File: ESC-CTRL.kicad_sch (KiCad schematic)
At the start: 42 parts, among them P1 V, P2 G, P3 TX, P4 RX, P5 D, P6 K, U1 AT32F413KCU7-4, U2 GM7333

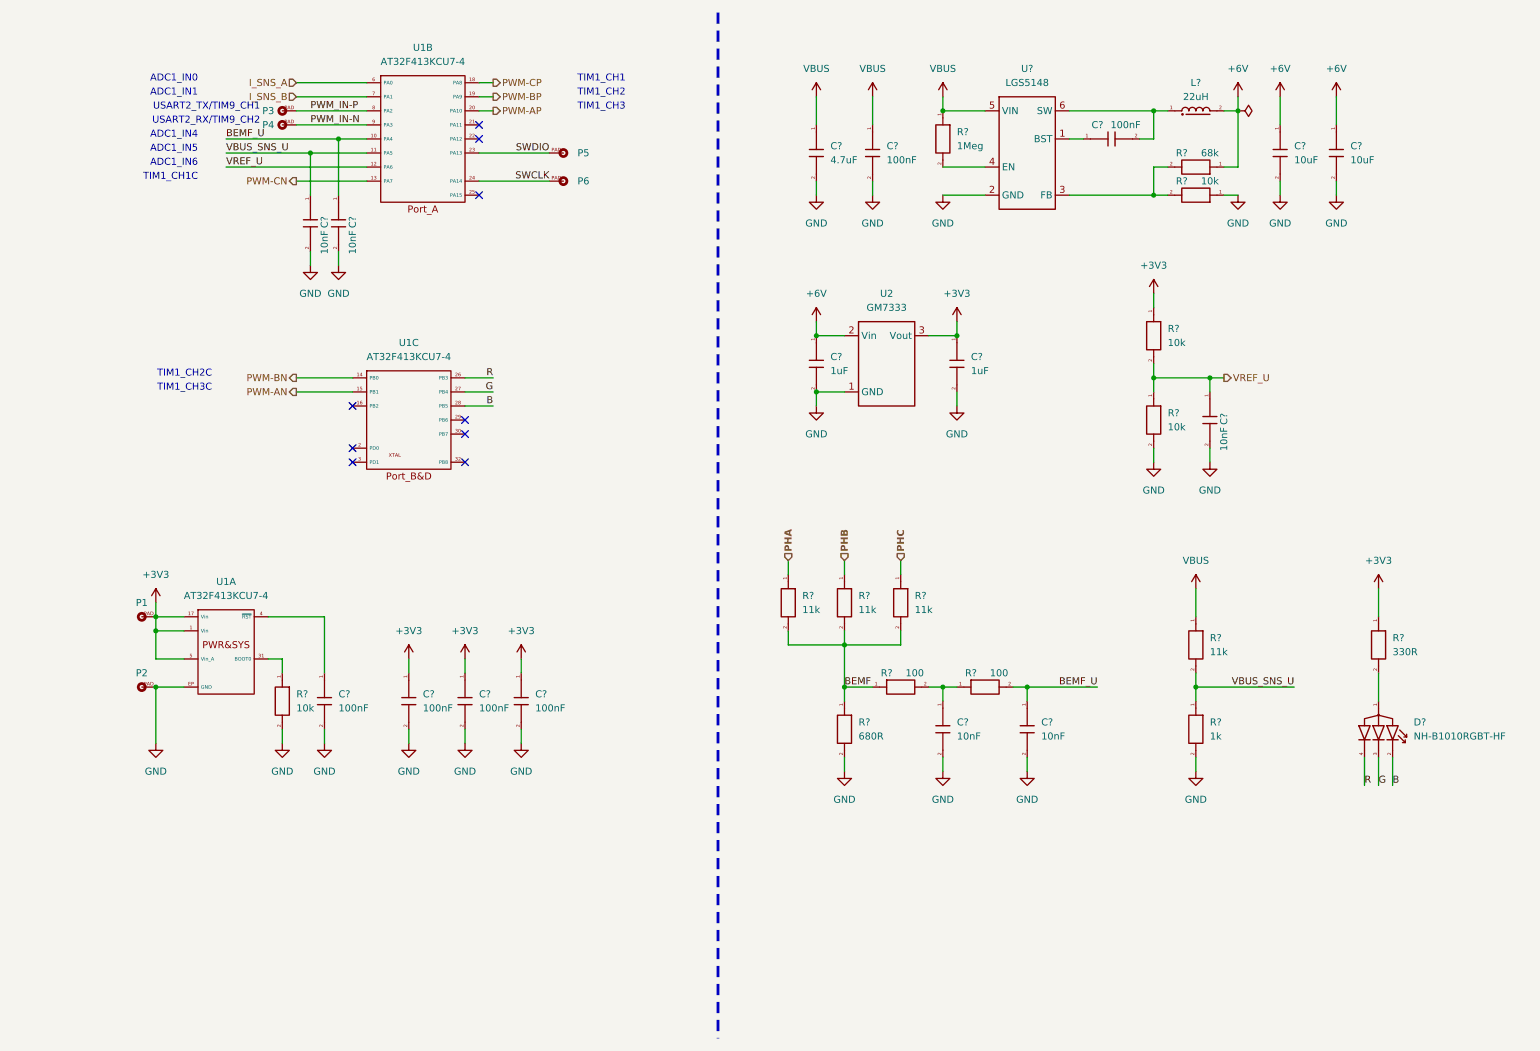
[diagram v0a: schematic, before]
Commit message: Update layout and modified sense amplifier
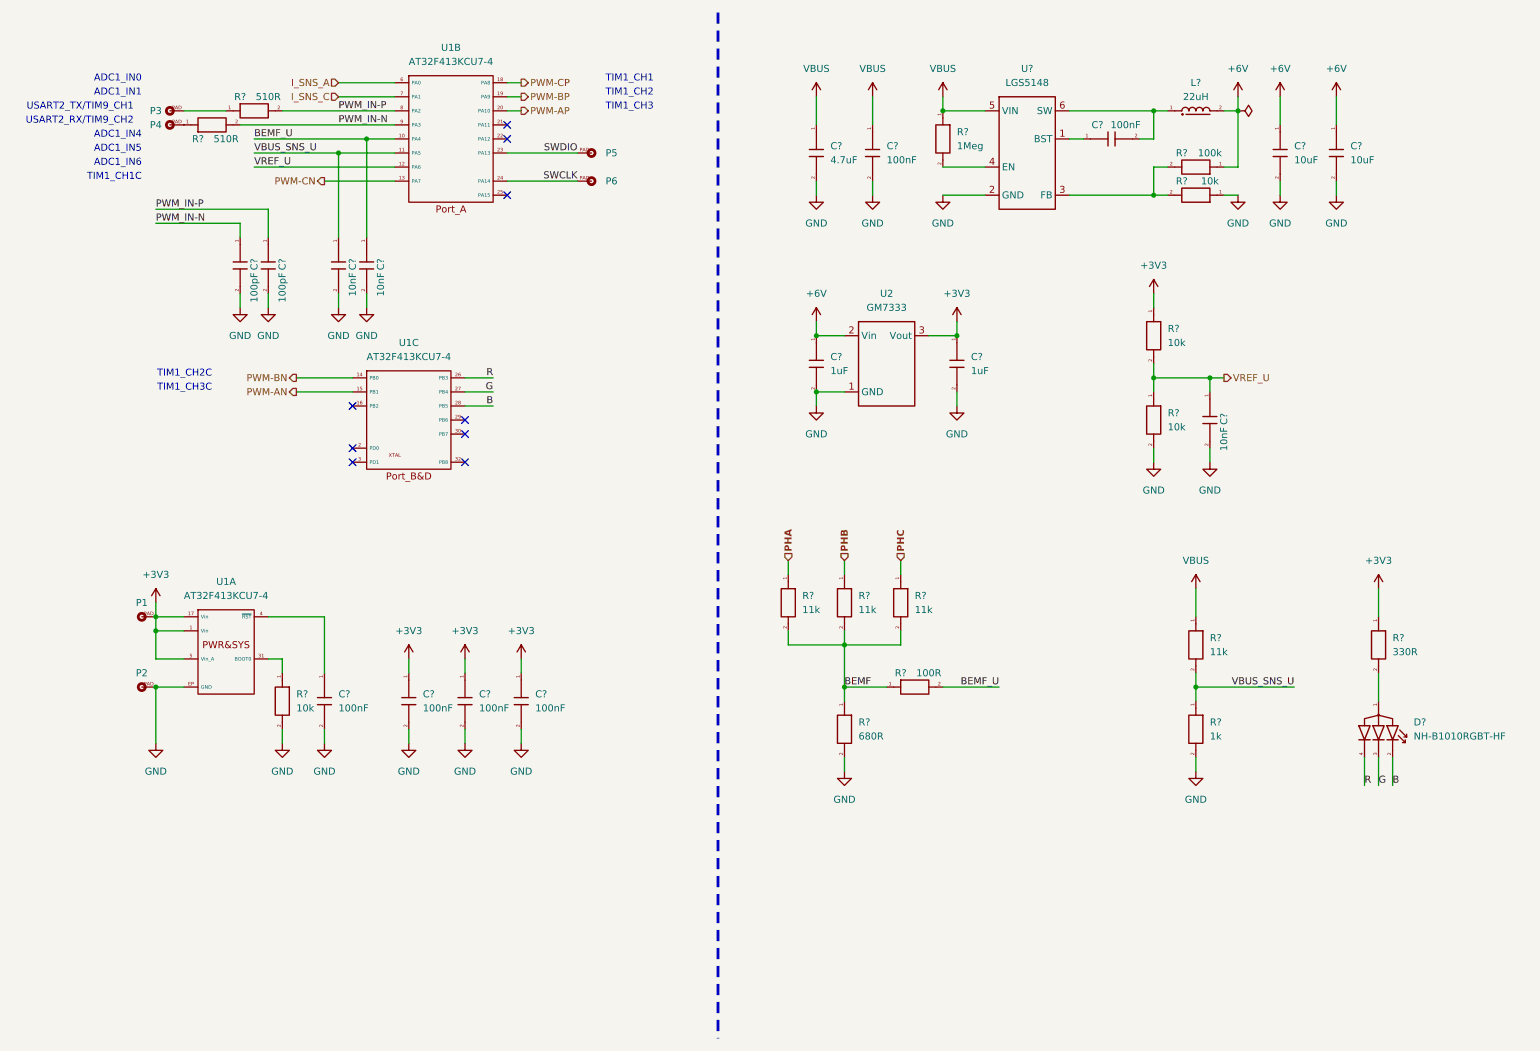
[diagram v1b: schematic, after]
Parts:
- removed C? (x2): 10nF, 001_GN_RCL_SMD:C0201(0603M), symbol 001_Basic_PassiveComponents:101_Capacitor
- removed R? (x2): 100, 001_GN_RCL_SMD:R0201(0603M), symbol 001_Basic_PassiveComponents:001_Resistor
- added C? (x2): 100pF, 001_GN_RCL_SMD:C0201(0603M), symbol 001_Basic_PassiveComponents:101_Capacitor
- added R?: 100R, 001_GN_RCL_SMD:R0201(0603M), symbol 001_Basic_PassiveComponents:001_Resistor
- added R? (x2): 510R, 001_GN_RCL_SMD:R0201(0603M), symbol 001_Basic_PassiveComponents:001_Resistor
- R?: value 68k -> 100k
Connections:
- net BEMF: now also R?.1
- net BEMF_U: now also R?.2
- net GND: now also C?.2, C?.2
- net PWM_IN-N: now also C?.1, R?.2; no longer P4.PAD
- net PWM_IN-P: now also C?.1, R?.2; no longer P3.PAD
- net I_SNS_B renamed I_SNS_C
- new net: P4.PAD, R?.1
- new net: P3.PAD, R?.1
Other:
- moved on the sheet: C?, P3, P4, P5, P6, U1B

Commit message: Modified the scheme of current sensing
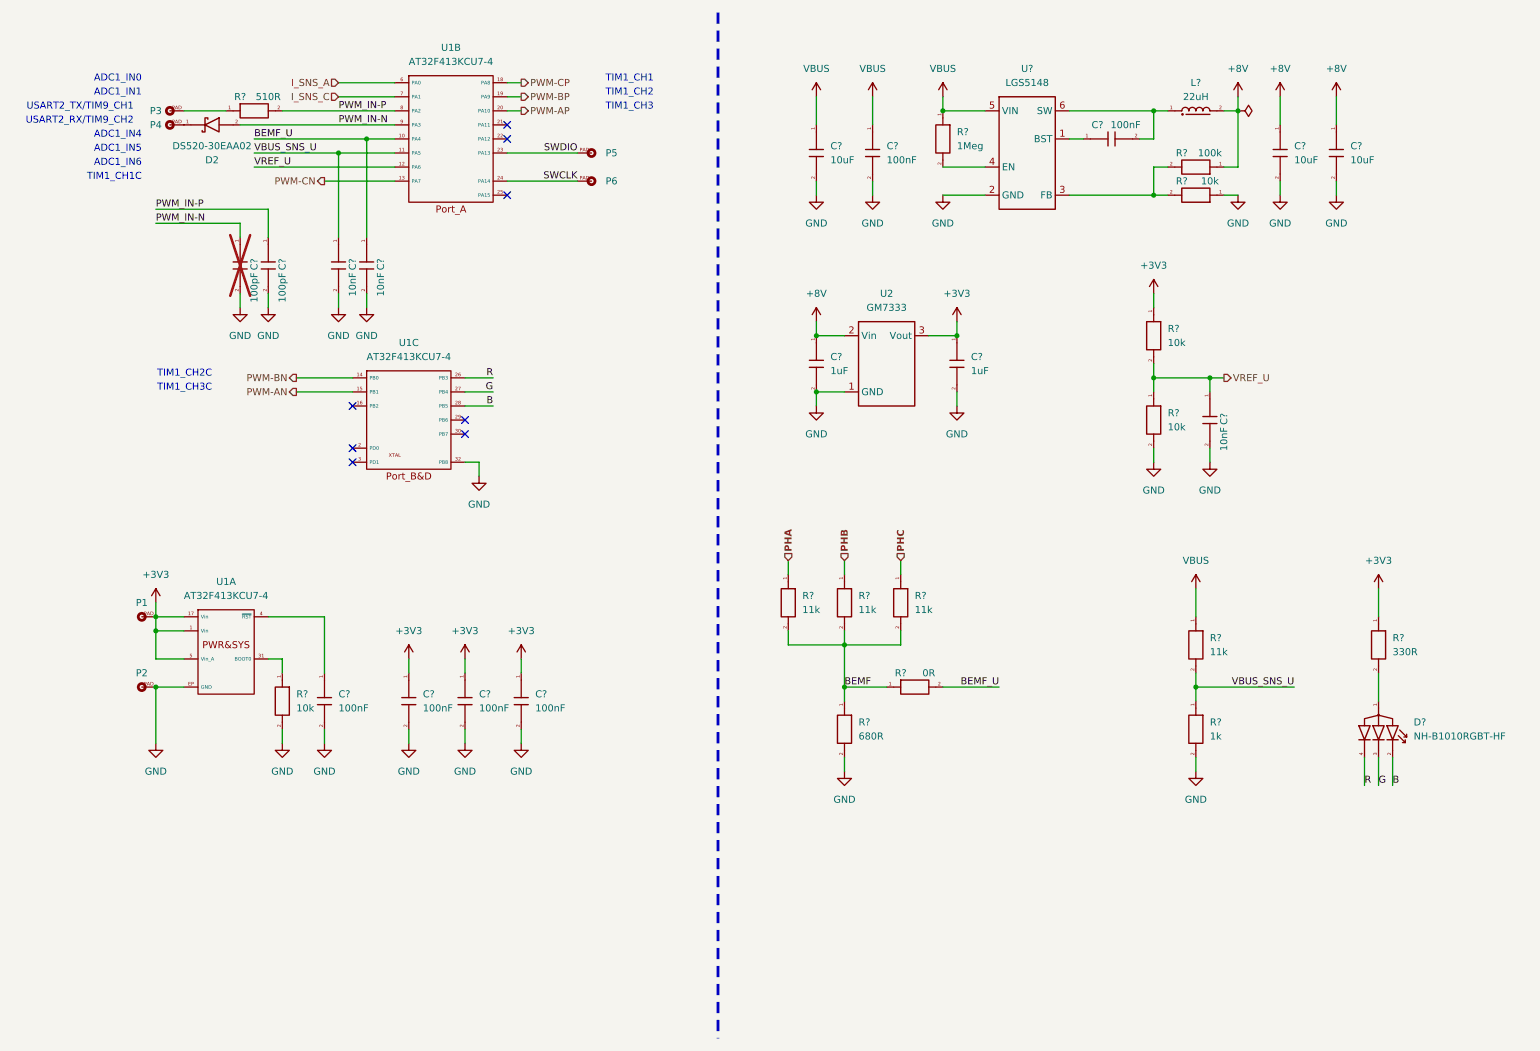
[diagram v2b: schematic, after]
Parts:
- removed R?: 510R, 001_GN_RCL_SMD:R0201(0603M), symbol 001_Basic_PassiveComponents:001_Resistor
- added D2: DS520-30EAA02, 002_GN_TWO-PIN_PLASTIC_SMD:DFN-2_1006, symbol 002_Basic_SingleSemiconductor:002_Diode_Schottky
- C?: value 4.7uF -> 10uF
- C?: now not fitted
- P1, P2, P3, P4, P5, P6: now left out of the parts list
- R?: value 100R -> 0R
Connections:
- net GND: now also U1.32 (PB8)
- net PWM_IN-N: now also D2.2 (Anode)
- net at P4.PAD: now also D2.1 (Cathode)
- net +6V renamed +8V
- no-connect marks 9 -> 8
